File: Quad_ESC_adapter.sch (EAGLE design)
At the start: 28 parts, among them Y1 ECS-80-S-4X

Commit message: complete connector placement
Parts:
- removed C10: 100nF, SparkFun-Capacitors:4.7UF0603
- removed C5, C6, C7, C8, C9: 4.7uF, SparkFun-Capacitors:4.7UF0603
- removed D1: (no value), SparkFun-LED:LED0603
- removed R1, R2, R3: 1k, SparkFun-Resistors:1KOHM-0603-1/10W-1%
- removed R4: 10k, SparkFun-Resistors:10KOHM-0603-1/10W-1%
- removed R7: (no value), SparkFun-Resistors:RESISTOR0603
- removed RESET: SWITCH, DiscreteComponents:SWITCH
- removed SV2: (no value), con-lsta:FE05-1
- removed U$1, U$5, U$6, U$7: 3PINCONNECTOR, BLHeli_32 45A:3PINCONNECTOR
- removed U$3: BACKPLANE_CONNECTORS, BLHeli_32 45A:BACKPLANE_CONNECTORS
- removed U$4: STM32F042K6T6, PI_Shield_Library:STM32F042K6T6
- removed U$8: TCAN337D, PI_Shield_Library:TCAN337D
- removed Y1: ECS-80-S-4X, ECS-80-S-4X:ECS-80-S-4X
- C1, C2, C3, C4: value 4.7uF -> 150uF; device SparkFun-Capacitors:4.7UF0603 -> Tantalum Cap 150 uF - Kemet 2917 T491:C-TANTALUM(10UF_150UF)
- U$2: value 8PIN_CONNECTOR -> BACKPLANE_ESC_ADAPTER_ESC; device BLHeli_32 45A:8PIN_CONNECTOR -> Backplane_ESC_adapter:BACKPLANE_ESC_ADAPTER_ESC
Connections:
- removed net +12V: U$10.VIN, U$3G$1.1, U$3G$1.2, U$3G$1.3, U$3G$1.4, U$3G$1.5, U$3G$1.6, U$3G$1.7, U$3G$1.8, U$3G$2.1, U$3G$2.2, U$3G$2.3, U$3G$2.4, U$3G$2.5, U$3G$2.6, U$3G$2.7, U$3G$2.8
- removed net +3V3: C1.1, C10.1, C2.1, C3.1, C4.1, C5.1, C6.1, R2.2, R4.1, SV2.5, U$2.LIPO_IN, U$3G$3.1, U$3G$3.2, U$3G$3.3, U$3G$3.4, U$4.VDD, U$4.VDDA, U$4.VDDIO2, U$8.VCC
- removed net CAN_H: U$3G$3.5, U$8.CANH
- removed net CAN_L: U$3G$3.7, U$8.CANL
- removed net CAN_RX: U$4.PA11, U$8.RXD
- removed net CAN_TX: U$4.PA12, U$8.TXD
- removed net LED: R7.2, U$4.PA15
- removed net N$1: C9.1, R1.1, Y1.2
- removed net N$2: C8.1, R3.1, Y1.1
- removed net N$24: D1.A, R7.1
- removed net N$3: R4.2, U$4.PA3
- removed net N$7: U$3G$3.8
- removed net N$8: U$3G$3.12
- removed net NRST: SV2.1, U$3G$3.6
- removed net NRST1: C7.1, R2.1, RESET.P$2, U$4.NRST
- removed net OSC_IN: R3.2, U$4.PF0-OSC_IN
- removed net OSC_OUT: R1.2, U$4.PF1-OSC_OUT
- removed net SWCLK: SV2.4, U$3G$3.11, U$4.PA14
- removed net SWDIO: SV2.2, U$3G$3.9, U$4.PA13
- removed net TIM3_CH1: U$2.MTR_1, U$4.PA6
- removed net TIM3_CH2: U$2.MTR_2, U$4.PA7
- removed net TIM3_CH3: U$2.MTR_3, U$4.PB0
- removed net TIM3_CH4: U$2.MTR_4, U$4.PB1
- removed net TLM: U$2.TLM, U$4.PA5
- new net 12V: C1.+, C2.+, C3.+, C4.+, U$10.VIN, U$2.VIN
- net ESC1_B: now also U$2.M1P1; no longer U$1.A
- net ESC1_R: now also U$2.M1P3; no longer U$1.C
- net ESC1_Y: now also U$2.M1P2; no longer U$1.B
- net ESC2_B: now also U$2.M2P1; no longer U$5.A
- net ESC2_R: now also U$2.M2P3; no longer U$5.C
- net ESC2_Y: now also U$2.M2P2; no longer U$5.B
- net ESC3_B: now also U$2.M3P1; no longer U$6.A
- net ESC3_R: now also U$2.M3P3; no longer U$6.C
- net ESC3_Y: now also U$2.M3P2; no longer U$6.B
- net ESC4_B: now also U$2.M4P1; no longer U$7.A
- net ESC4_R: now also U$2.M4P3; no longer U$7.C
- net ESC4_Y: now also U$2.M4P2; no longer U$7.B
- net GND: now also C1.-, C2.-, C3.-, C4.-, U$2.GND; no longer C1.2, C10.2, C2.2, C3.2, C4.2, C5.2, C6.2, C7.2, C8.2, C9.2, D1.C, RESET.P$1, SV2.3, U$2.ADC, U$2.LIPO_GND, U$3G$1.10, U$3G$1.11, U$3G$1.12, U$3G$1.9, U$3G$2.10, U$3G$2.11, U$3G$2.12, U$3G$2.9, U$4.PB8-BOOT0, U$4.VSS, U$4.VSS1, U$8.GND
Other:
- note added: "LUMENIER ESC"
- note removed: "CAN TRANSCEIVER"
- note removed: "ID resistor to backplane"
- note removed: "LUMENIER ESC & 8 PIN CONNECTOR"
- note removed: "M1 3 Pin"
- note removed: "M2 3 Pin"
- note removed: "M3 3 Pin"
- note removed: "M4 3 Pin"
- note removed: "MOTOR 3PIN CONNECTORS"
- note removed: "PROGRAMMING HEADERS"
- note removed: "STM32F042K6T6"

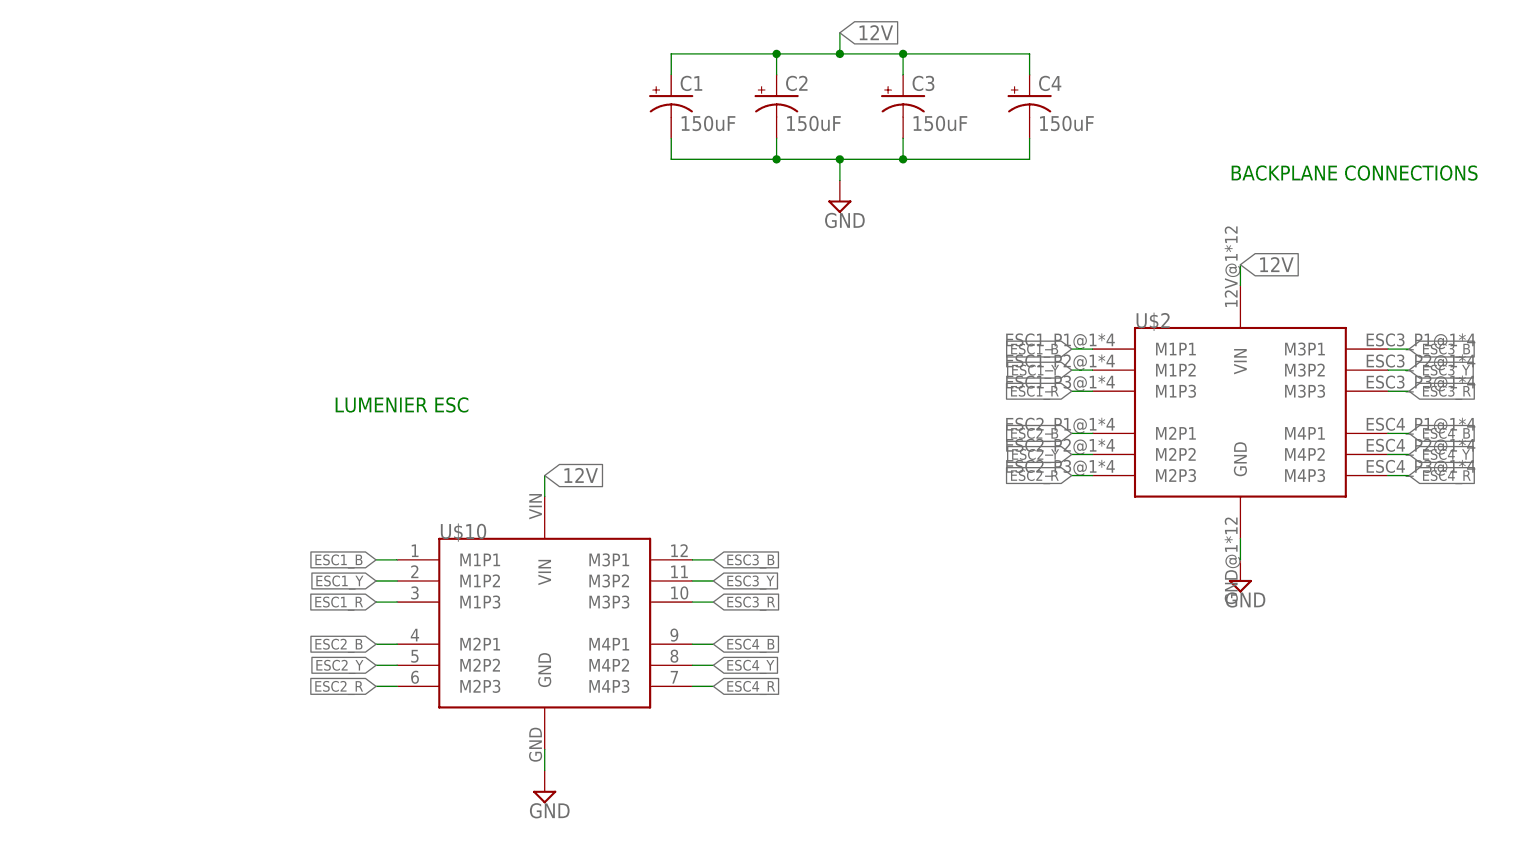
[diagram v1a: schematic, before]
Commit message: routed wider board
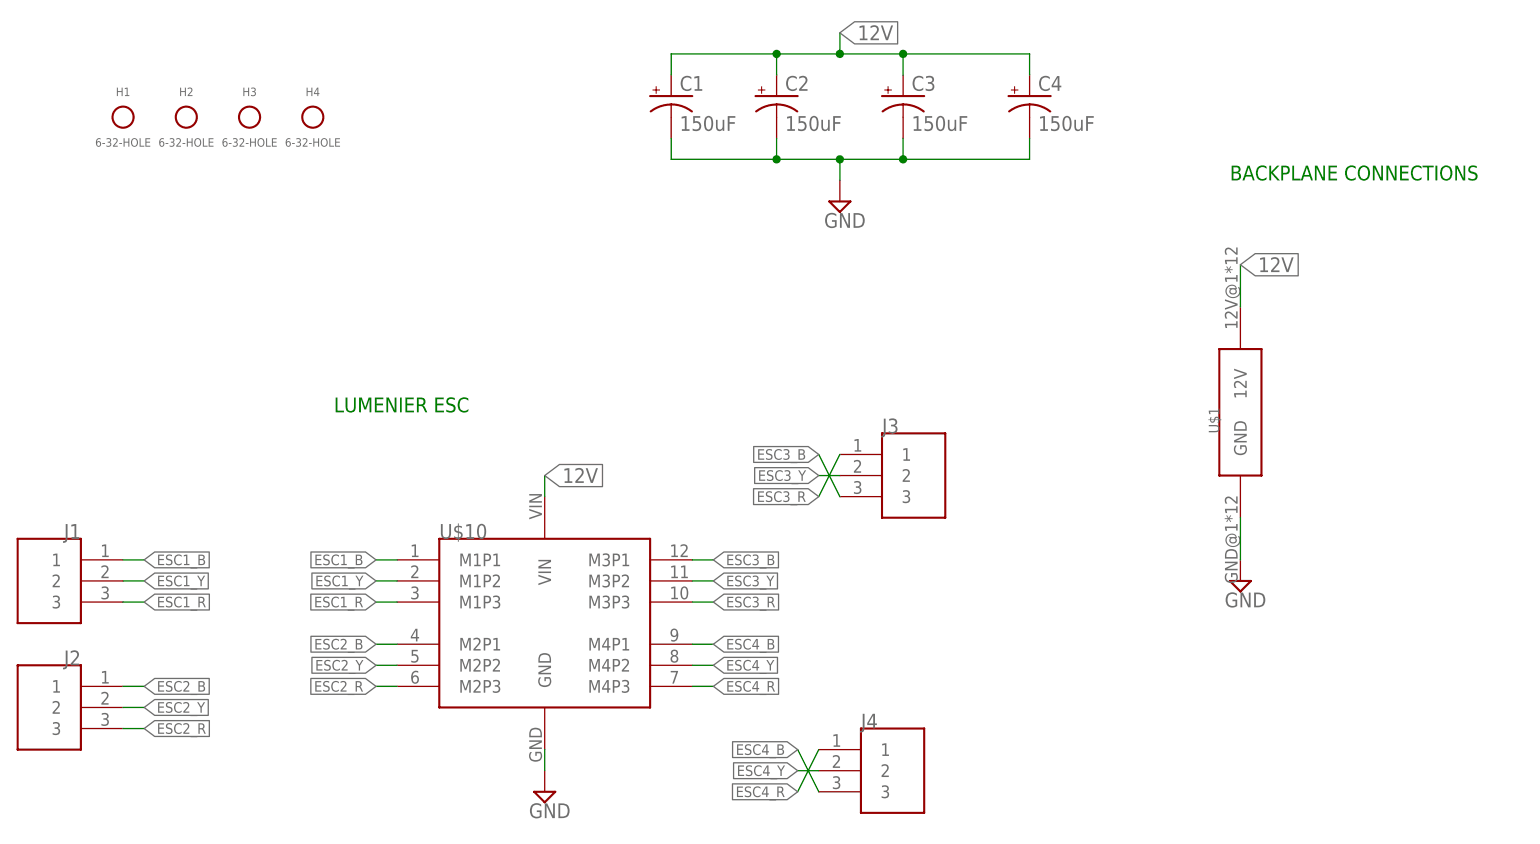
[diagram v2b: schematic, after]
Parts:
- removed U$2: BACKPLANE_ESC_ADAPTER_ESC, Backplane_ESC_adapter:BACKPLANE_ESC_ADAPTER_ESC
- added H1, H2, H3, H4: 6-32-HOLE, Mounting Holes:6-32-HOLE
- added J1, J2, J3, J4: 284512-3, ThrusterConnector:284512-3
- added U$1: BACKPLANE_ESC_ADAPTER_ESC_PWR, Backplane_ESC_adapter:BACKPLANE_ESC_ADAPTER_ESC_PWR
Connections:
- net 12V: now also U$1.12V; no longer U$2.VIN
- net ESC1_B: now also J1.1; no longer U$2.M1P1
- net ESC1_R: now also J1.3; no longer U$2.M1P3
- net ESC1_Y: now also J1.2; no longer U$2.M1P2
- net ESC2_B: now also J2.1; no longer U$2.M2P1
- net ESC2_R: now also J2.3; no longer U$2.M2P3
- net ESC2_Y: now also J2.2; no longer U$2.M2P2
- net ESC3_B: now also J3.3; no longer U$2.M3P1
- net ESC3_R: now also J3.1; no longer U$2.M3P3
- net ESC3_Y: now also J3.2; no longer U$2.M3P2
- net ESC4_B: now also J4.3; no longer U$2.M4P1
- net ESC4_R: now also J4.1; no longer U$2.M4P3
- net ESC4_Y: now also J4.2; no longer U$2.M4P2
- net GND: now also U$1.GND; no longer U$2.GND

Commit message: routed with 2x12 block. Basically ready to order
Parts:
- removed U$1: BACKPLANE_ESC_ADAPTER_ESC_PWR, Backplane_ESC_adapter:BACKPLANE_ESC_ADAPTER_ESC_PWR
- added U$2: BACKPLANE_ESC_ADAPTER_PWRESC, Backplane_ESC_adapter:BACKPLANE_ESC_ADAPTER_PWRESC
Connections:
- net 12V: now also U$2.12V; no longer U$1.12V
- net ESC1_B: now also J1.3; no longer J1.1
- net ESC1_R: now also J1.1; no longer J1.3
- net ESC2_B: now also J2.3; no longer J2.1
- net ESC2_R: now also J2.1; no longer J2.3
- net ESC3_B: now also J3.1; no longer J3.3
- net ESC3_R: now also J3.3; no longer J3.1
- net ESC4_B: now also J4.1; no longer J4.3
- net ESC4_R: now also J4.3; no longer J4.1
- net GND: now also U$2.GND; no longer U$1.GND
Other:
- moved on the sheet: C4, H3, H4
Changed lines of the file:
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@@
 <part name="H3" library="Mounting Holes" deviceset="6-32-HOLE" device="" package3d_urn="urn:adsk.eagle:package:24384748/2"/>
 <part name="H4" library="Mounting Holes" deviceset="6-32-HOLE" device="" package3d_urn="urn:adsk.eagle:package:24384748/2"/>
-<part name="U$1" library="Backplane_ESC_adapter" deviceset="BACKPLANE_ESC_ADAPTER_ESC_PWR" device=""/>
+<part name="U$2" library="Backplane_ESC_adapter" deviceset="BACKPLANE_ESC_ADAPTER_PWR" device="ESC"/>
 </parts>
 <sheets>
@@
 <plain>
 <text x="209.55" y="91.44" size="1.778" layer="91">BACKPLANE CONNECTIONS</text>
-<text x="101.6" y="63.5" size="1.778" layer="91">LUMENIER ESC</text>
+<text x="114.3" y="60.96" size="1.778" layer="91">LUMENIER ESC</text>
 </plain>
 <instances>
@@
 <attribute name="VALUE" x="171.196" y="97.409" size="1.778" layer="96"/>
 </instance>
-<instance part="C4" gate="G$1" x="185.42" y="101.6" smashed="yes">
-<attribute name="NAME" x="186.436" y="102.235" size="1.778" layer="95"/>
-<attribute name="VALUE" x="186.436" y="97.409" size="1.778" layer="96"/>
+<instance part="C4" gate="G$1" x="182.88" y="101.6" smashed="yes">
+<attribute name="NAME" x="183.896" y="102.235" size="1.778" layer="95"/>
+<attribute name="VALUE" x="183.896" y="97.409" size="1.778" layer="96"/>
 </instance>
 <instance part="SUPPLY1" gate="GND" x="162.56" y="88.9" smashed="yes">
@@
 <attribute name="VALUE" x="83.82" y="96.52" size="1.016" layer="95" align="top-center"/>
 </instance>
-<instance part="H3" gate="G$1" x="91.44" y="99.06" smashed="yes">
-<attribute name="NAME" x="91.44" y="101.6" size="1.016" layer="95" align="bottom-center"/>
-<attribute name="VALUE" x="91.44" y="96.52" size="1.016" layer="95" align="top-center"/>
-</instance>
-<instance part="H4" gate="G$1" x="99.06" y="99.06" smashed="yes">
-<attribute name="NAME" x="99.06" y="101.6" size="1.016" layer="95" align="bottom-center"/>
-<attribute name="VALUE" x="99.06" y="96.52" size="1.016" layer="95" align="top-center"/>
-</instance>
-<instance part="U$1" gate="G$1" x="210.82" y="63.5" smashed="yes">
+<instance part="H3" gate="G$1" x="76.2" y="88.9" smashed="yes">
+<attribute name="NAME" x="76.2" y="91.44" size="1.016" layer="95" align="bottom-center"/>
+<attribute name="VALUE" x="76.2" y="86.36" size="1.016" layer="95" align="top-center"/>
+</instance>
+<instance part="H4" gate="G$1" x="83.82" y="88.9" smashed="yes">
+<attribute name="NAME" x="83.82" y="91.44" size="1.016" layer="95" align="bottom-center"/>
+<attribute name="VALUE" x="83.82" y="86.36" size="1.016" layer="95" align="top-center"/>
+</instance>
+<instance part="U$2" gate="G$1" x="210.82" y="63.5" smashed="yes">
 <attribute name="NAME" x="208.28" y="60.96" size="1.27" layer="95" rot="R90"/>
 </instance>
@@
 <wire x1="154.94" y1="93.98" x2="162.56" y2="93.98" width="0.1524" layer="91"/>
 <wire x1="162.56" y1="93.98" x2="170.18" y2="93.98" width="0.1524" layer="91"/>
-<wire x1="170.18" y1="93.98" x2="185.42" y2="93.98" width="0.1524" layer="91"/>
-<wire x1="185.42" y1="93.98" x2="185.42" y2="96.52" width="0.1524" layer="91"/>
+<wire x1="170.18" y1="93.98" x2="182.88" y2="93.98" width="0.1524" layer="91"/>
+<wire x1="182.88" y1="93.98" x2="182.88" y2="96.52" width="0.1524" layer="91"/>
 <pinref part="C3" gate="G$1" pin="-"/>
 <wire x1="170.18" y1="96.52" x2="170.18" y2="93.98" width="0.1524" layer="91"/>
@@
 <pinref part="SUPPLY4" gate="GND" pin="GND"/>
 <wire x1="210.82" y1="45.72" x2="210.82" y2="50.8" width="0.1524" layer="91"/>
-<pinref part="U$1" gate="G$1" pin="GND"/>
+<pinref part="U$2" gate="G$1" pin="GND"/>
 </segment>
 </net>
@@
 </segment>
 <segment>
-<wire x1="160.02" y1="17.78" x2="157.48" y2="22.86" width="0.1524" layer="91"/>
+<wire x1="160.02" y1="22.86" x2="157.48" y2="22.86" width="0.1524" layer="91"/>
 <label x="157.48" y="22.86" size="1.27" layer="95" rot="MR0" xref="yes"/>
-<pinref part="J4" gate="G$1" pin="3"/>
+<pinref part="J4" gate="G$1" pin="1"/>
 </segment>
 </net>
@@
 </segment>
 <segment>
-<wire x1="160.02" y1="22.86" x2="157.48" y2="17.78" width="0.1524" layer="91"/>
+<wire x1="160.02" y1="17.78" x2="157.48" y2="17.78" width="0.1524" layer="91"/>
 <label x="157.48" y="17.78" size="1.27" layer="95" rot="MR0" xref="yes"/>
-<pinref part="J4" gate="G$1" pin="1"/>
+<pinref part="J4" gate="G$1" pin="3"/>
 </segment>
 </net>
@@
 </segment>
 <segment>
-<wire x1="162.56" y1="53.34" x2="160.02" y2="58.42" width="0.1524" layer="91"/>
+<wire x1="162.56" y1="58.42" x2="160.02" y2="58.42" width="0.1524" layer="91"/>
 <label x="160.02" y="58.42" size="1.27" layer="95" rot="MR0" xref="yes"/>
-<pinref part="J3" gate="G$1" pin="3"/>
+<pinref part="J3" gate="G$1" pin="1"/>
 </segment>
 </net>
@@
 </segment>
 <segment>
-<wire x1="162.56" y1="58.42" x2="160.02" y2="53.34" width="0.1524" layer="91"/>
+<wire x1="162.56" y1="53.34" x2="160.02" y2="53.34" width="0.1524" layer="91"/>
 <label x="160.02" y="53.34" size="1.27" layer="95" rot="MR0" xref="yes"/>
-<pinref part="J3" gate="G$1" pin="1"/>
+<pinref part="J3" gate="G$1" pin="3"/>
 </segment>
 </net>
@@
 </segment>
 <segment>
+<wire x1="76.2" y1="25.4" x2="78.74" y2="25.4" width="0.1524" layer="91"/>
+<label x="78.74" y="25.4" size="1.27" layer="95" rot="MR180" xref="yes"/>
+<pinref part="J2" gate="G$1" pin="3"/>
+</segment>
+</net>
+<net name="ESC2_Y" class="0">
+<segment>
+<pinref part="U$10" gate="G$1" pin="M2P2"/>
+<wire x1="109.22" y1="33.02" x2="106.68" y2="33.02" width="0.1524" layer="91"/>
+<label x="106.68" y="33.02" size="1.27" layer="95" rot="R180" xref="yes"/>
+</segment>
+<segment>
+<wire x1="76.2" y1="27.94" x2="78.74" y2="27.94" width="0.1524" layer="91"/>
+<label x="78.74" y="27.94" size="1.27" layer="95" rot="MR180" xref="yes"/>
+<pinref part="J2" gate="G$1" pin="2"/>
+</segment>
+</net>
+<net name="ESC2_R" class="0">
+<segment>
+<pinref part="U$10" gate="G$1" pin="M2P3"/>
+<wire x1="109.22" y1="30.48" x2="106.68" y2="30.48" width="0.1524" layer="91"/>
+<label x="106.68" y="30.48" size="1.27" layer="95" rot="R180" xref="yes"/>
+</segment>
+<segment>
 <wire x1="76.2" y1="30.48" x2="78.74" y2="30.48" width="0.1524" layer="91"/>
 <label x="78.74" y="30.48" size="1.27" layer="95" rot="MR180" xref="yes"/>
@@
 </segment>
 </net>
-<net name="ESC2_Y" class="0">
-<segment>
-<pinref part="U$10" gate="G$1" pin="M2P2"/>
-<wire x1="109.22" y1="33.02" x2="106.68" y2="33.02" width="0.1524" layer="91"/>
-<label x="106.68" y="33.02" size="1.27" layer="95" rot="R180" xref="yes"/>
-</segment>
-<segment>
-<wire x1="76.2" y1="27.94" x2="78.74" y2="27.94" width="0.1524" layer="91"/>
-<label x="78.74" y="27.94" size="1.27" layer="95" rot="MR180" xref="yes"/>
-<pinref part="J2" gate="G$1" pin="2"/>
-</segment>
-</net>
-<net name="ESC2_R" class="0">
-<segment>
-<pinref part="U$10" gate="G$1" pin="M2P3"/>
-<wire x1="109.22" y1="30.48" x2="106.68" y2="30.48" width="0.1524" layer="91"/>
-<label x="106.68" y="30.48" size="1.27" layer="95" rot="R180" xref="yes"/>
-</segment>
-<segment>
-<wire x1="76.2" y1="25.4" x2="78.74" y2="25.4" width="0.1524" layer="91"/>
-<label x="78.74" y="25.4" size="1.27" layer="95" rot="MR180" xref="yes"/>
-<pinref part="J2" gate="G$1" pin="3"/>
-</segment>
-</net>
 <net name="ESC1_Y" class="0">
 <segment>
@@
 </segment>
 <segment>
-<wire x1="76.2" y1="40.64" x2="78.74" y2="40.64" width="0.1524" layer="91"/>
-<label x="78.74" y="40.64" size="1.27" layer="95" rot="MR180" xref="yes"/>
-<pinref part="J1" gate="G$1" pin="3"/>
+<wire x1="76.2" y1="45.72" x2="78.74" y2="45.72" width="0.1524" layer="91"/>
+<label x="78.74" y="45.72" size="1.27" layer="95" rot="MR180" xref="yes"/>
+<pinref part="J1" gate="G$1" pin="1"/>
 </segment>
 </net>
@@
 <wire x1="154.94" y1="106.68" x2="162.56" y2="106.68" width="0.1524" layer="91"/>
 <wire x1="162.56" y1="106.68" x2="170.18" y2="106.68" width="0.1524" layer="91"/>
-<wire x1="170.18" y1="106.68" x2="185.42" y2="106.68" width="0.1524" layer="91"/>
-<wire x1="185.42" y1="106.68" x2="185.42" y2="104.14" width="0.1524" layer="91"/>
+<wire x1="170.18" y1="106.68" x2="182.88" y2="106.68" width="0.1524" layer="91"/>
+<wire x1="182.88" y1="106.68" x2="182.88" y2="104.14" width="0.1524" layer="91"/>
 <pinref part="C3" gate="G$1" pin="+"/>
 <wire x1="170.18" y1="104.14" x2="170.18" y2="106.68" width="0.1524" layer="91"/>
@@
 <wire x1="210.82" y1="76.2" x2="210.82" y2="81.28" width="0.1524" layer="91"/>
 <label x="210.82" y="81.28" size="1.778" layer="95" xref="yes"/>
-<pinref part="U$1" gate="G$1" pin="12V"/>
+<pinref part="U$2" gate="G$1" pin="12V"/>
 </segment>
 </net>
@@
 </segment>
 <segment>
-<wire x1="76.2" y1="45.72" x2="78.74" y2="45.72" width="0.1524" layer="91"/>
-<label x="78.74" y="45.72" size="1.27" layer="95" rot="MR180" xref="yes"/>
-<pinref part="J1" gate="G$1" pin="1"/>
-</segment>
-</net>
+<wire x1="76.2" y1="40.64" x2="78.74" y2="40.64" width="0.1524" layer="91"/>
+<label x="78.74" y="40.64" size="1.27" layer="95" rot="MR180" xref="yes"/>
+<pinref part="J1" gate="G$1" pin="3"/>
+</segment>
+</net>

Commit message: single outline version
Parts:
- U$10: value LUMENIER_QUAD -> LUMENIER_QUAD-NO-CUT; device BLHeli_32 45A:LUMENIER_QUAD -> Lumenier ESC:LUMENIER_QUAD-NO-CUT
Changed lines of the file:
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@@
 <parts>
 <part name="FRAME1" library="SparkFun-Aesthetics" library_urn="urn:adsk.eagle:library:507" deviceset="FRAME-A4L" device=""/>
-<part name="U$10" library="BLHeli_32 45A" deviceset="LUMENIER_QUAD" device="" package3d_urn="urn:adsk.eagle:package:24294694/3"/>
+<part name="U$10" library="Lumenier ESC" deviceset="LUMENIER_QUAD-NO-CUT" device="" package3d_urn="urn:adsk.eagle:package:24294694/3"/>
 <part name="SUPPLY5" library="supply2" library_urn="urn:adsk.eagle:library:372" deviceset="GND" device=""/>
 <part name="C1" library="Tantalum Cap 150 uF - Kemet 2917 T491" deviceset="C-TANTALUM(10UF_150UF)" device="" package3d_urn="urn:adsk.eagle:package:25131320/3" value="150uF"/>
